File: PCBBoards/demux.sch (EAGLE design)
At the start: 106 parts, among them IC1 4013N, IC2 4013N, IC3 4013N, IC4 4013N, IC5 4013N, IC6 4013N, IC7 4069N, IC8 4069N, Q1 2N3904, Q10 2N3904, Q11 2N3904, Q12 2N3904, Q2 2N3904, Q3 2N3904, Q4 2N3904, Q5 2N3904, Q6 2N3904, Q7 2N3904, Q8 2N3904, Q9 2N3904, T1 2N3904, T2 2N3904, T3 2N3904, T4 2N3904, T5 2N3904, T6 2N3904

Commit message: fr/sr another one
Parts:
- removed C2, C3, C4, C5, C6, C7, C8, C9: 100n, rcl:C-EU050-035X075
- C1: value 100n -> 1u
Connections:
- new net N$80: IC6B.CLK, IC8D.O
- new net N$81: IC8D.I
- net +5V: no longer C2.1, C3.1, C4.1, C5.1, C6.1, C7.2, C8.1, C9.1
- net GND: no longer C2.2, C3.2, C4.2, C5.2, C6.2, C7.1, C8.2, C9.2
- net N$11: now also IC5B.CLK; no longer IC6B.CLK
- net N$2: now also IC7F.O; no longer IC7D.O
- net N$27: now also IC7F.I; no longer IC7D.I
- net N$29: now also IC7D.I; no longer IC7F.I
- net N$33: no longer IC8D.I
- net N$35: no longer IC8F.I
- net N$5: now also IC7D.O; no longer IC7F.O
- net N$9: now also IC8F.I; no longer IC5B.CLK, IC8D.O
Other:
- moved on the sheet: IC7D, IC7F, IC8D, IC8F

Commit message: first version of complited FR/SR PCB board
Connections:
- removed net N$24: IC7A.I, V11.0
- removed net N$3 (its old number): IC2A.CLK, IC7C.O
- removed net N$80: IC6B.CLK, IC8D.O
- removed net N$81: IC8D.I
- new net N$4: IC1A.CLK, IC7E.O
- new net N$82: IC8E.I, V11.8
- net N$1: now also IC2A.CLK, IC7F.O; no longer IC3A.CLK, IC7E.O
- net N$10: now also IC8B.I, V11.9; no longer IC6A.CLK, IC8E.O
- net N$11: now also IC6A.CLK, IC8D.O; no longer IC5B.CLK, IC8F.O
- net N$13: now also IC3B.CLK, IC7C.O; no longer IC1A.CLK, IC7A.O
- net N$2: now also IC7A.O; no longer IC7F.O
- net N$26: now also IC7F.I; no longer IC7C.I
- net N$27: now also IC7A.I; no longer IC7F.I
- net N$28: now also IC7D.I; no longer IC7E.I
- net N$29: now also IC7C.I; no longer IC7D.I
- net N$30: now also IC8F.I; no longer IC8A.I
- net N$31: now also IC8A.I; no longer IC8B.I
- net N$32: now also IC5B.CLK, IC8B.O; no longer IC8C.I, V11.8
- net N$33: now also IC5A.CLK, IC8E.O; no longer V11.9
- net N$34: now also IC8D.I; no longer IC8E.I
- net N$35: now also IC8C.I
- net N$5: now also IC7E.I, V11.0; no longer IC3B.CLK, IC7D.O
- net N$6: now also IC8F.O; no longer IC8A.O
- net N$7: now also IC8A.O; no longer IC8B.O
- net N$8: now also IC3A.CLK, IC7D.O; no longer IC5A.CLK, IC8C.O
- net N$9: now also IC6B.CLK, IC8C.O; no longer IC8F.I
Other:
- moved on the sheet: IC7A, IC7B, IC7C, IC7D, IC7E, IC7F, IC8A, IC8B, IC8C, IC8D, IC8E, IC8F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

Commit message: FR/RS Board one of final update
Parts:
- added C2, C3, C4, C5, C6, C7, C8, C9: 100n, rcl:C-EU025-025X050
- C1: value 1u -> 100n; device rcl:C-EU050-035X075 -> rcl:C-EU025-025X050
- R19, R24, R25, R28, R33, R34: value 15k -> 4.7k
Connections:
- net +5V: now also C2.1, C3.1, C4.1, C5.1, C6.1, C7.1, C8.1, C9.1
- net GND: now also C2.2, C3.2, C4.2, C5.2, C6.2, C7.2, C8.2, C9.2

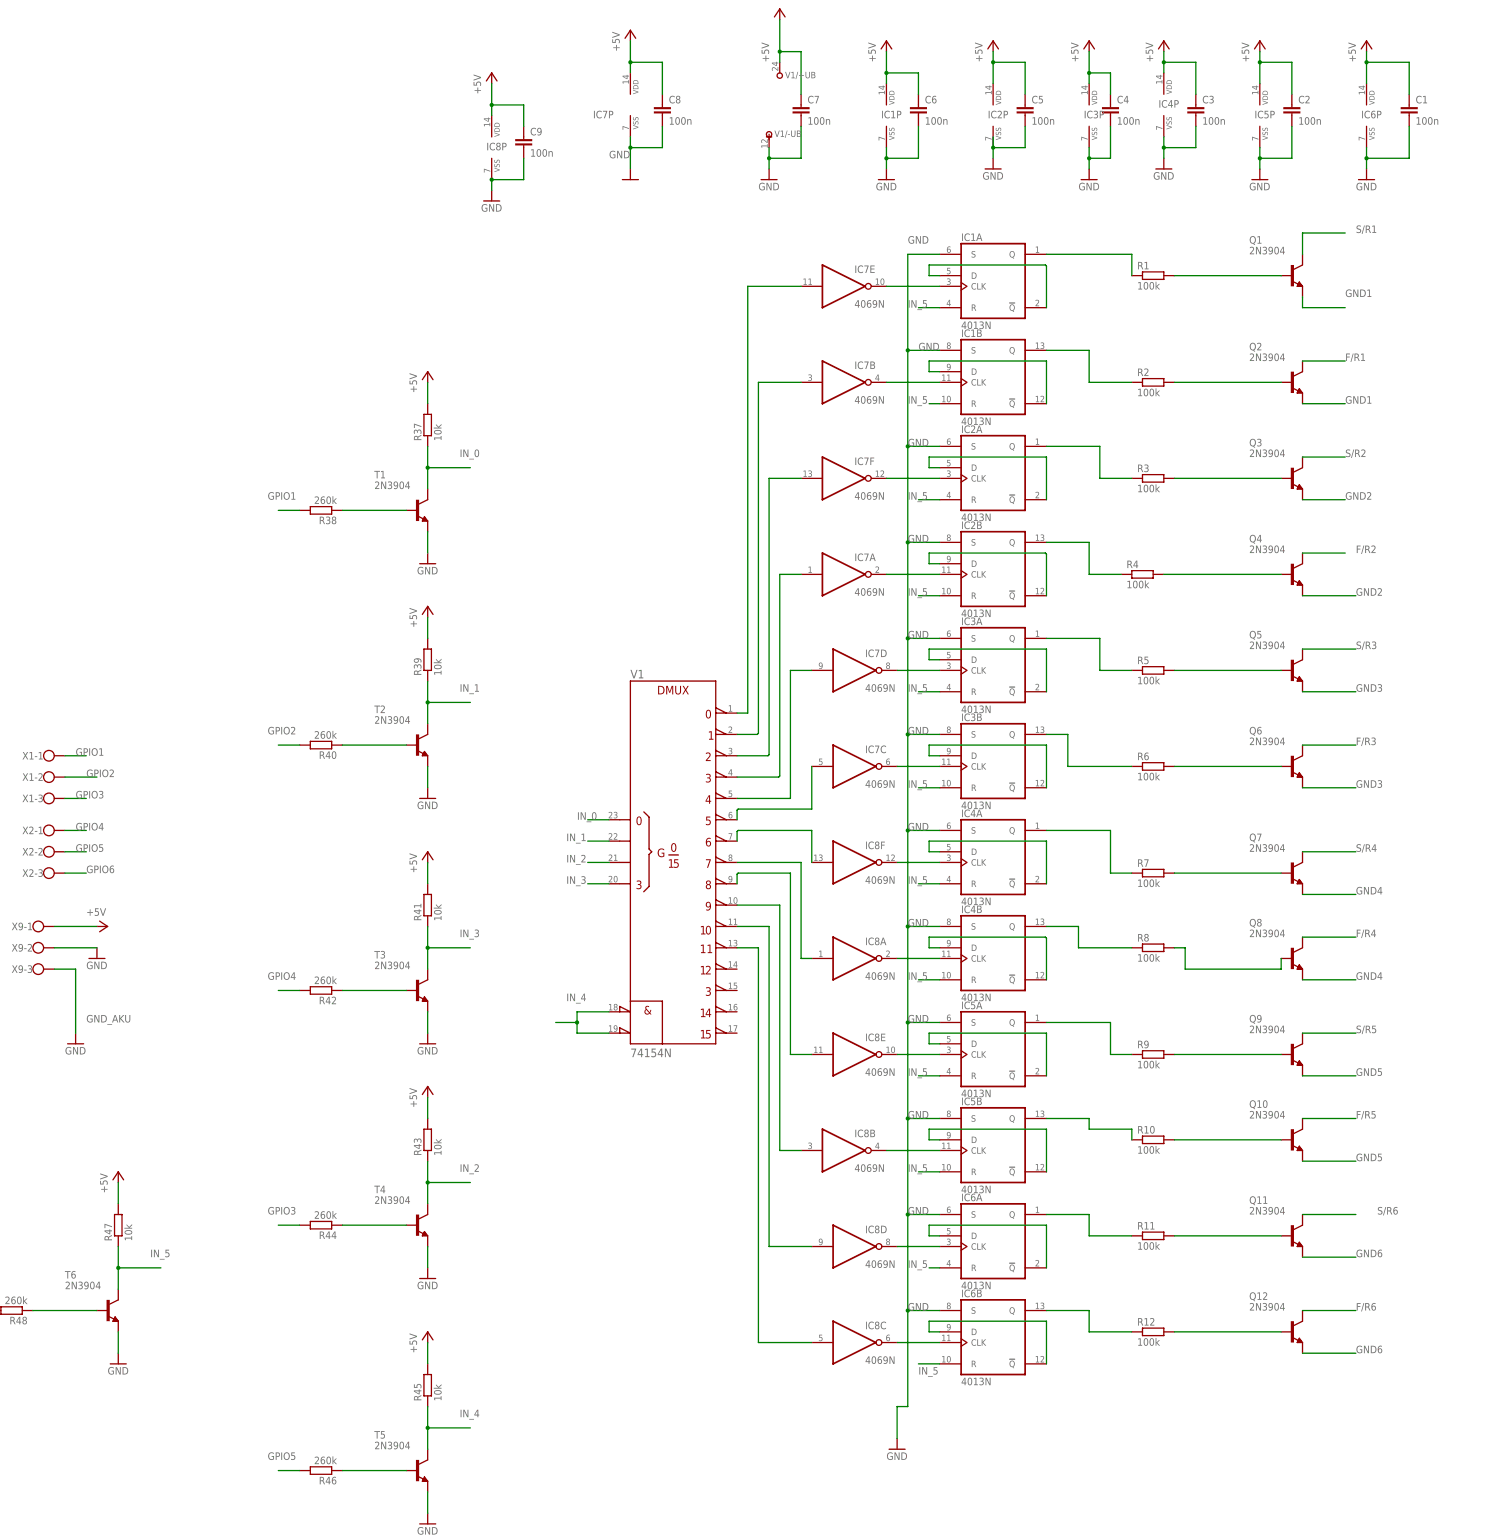
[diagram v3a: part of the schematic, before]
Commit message: FR/SR updated to 74HC**
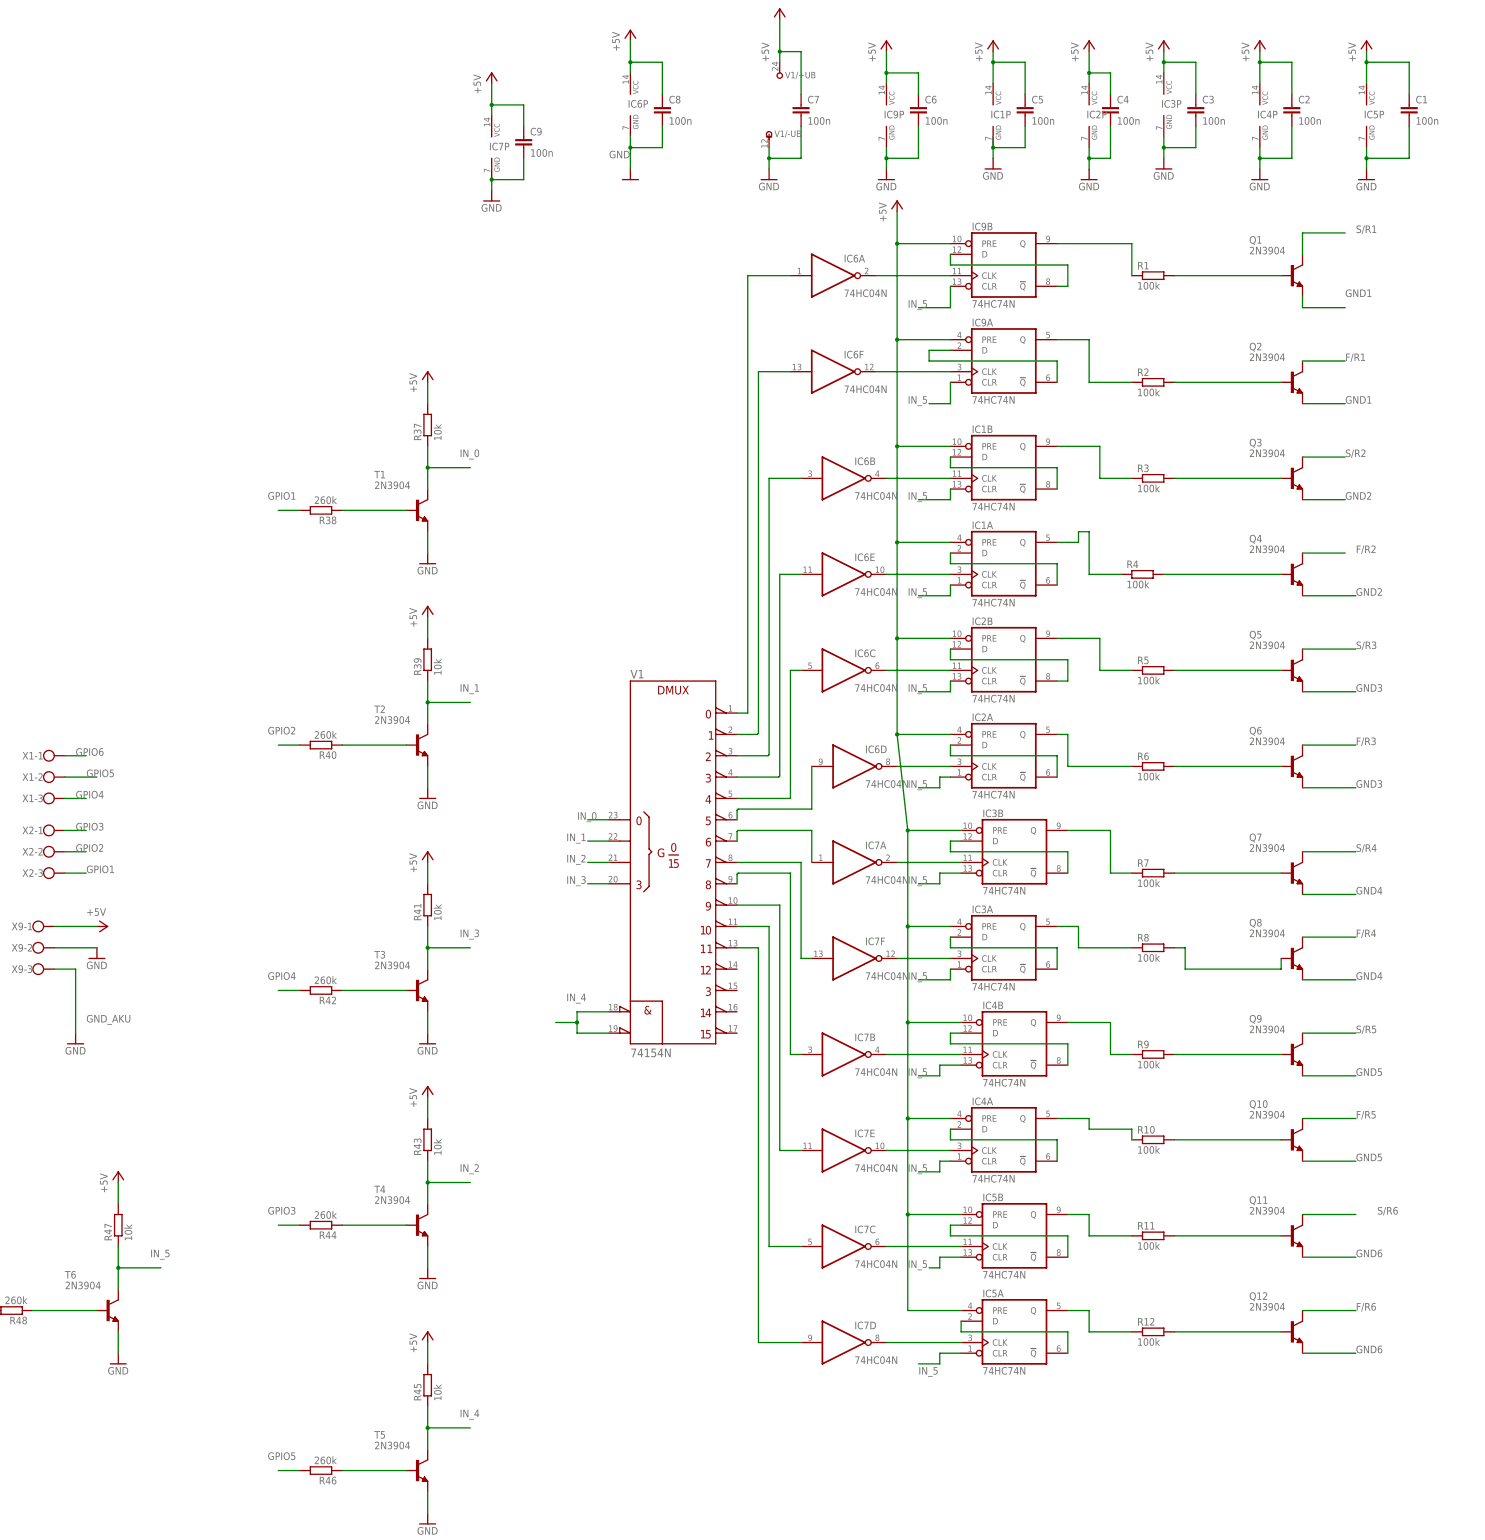
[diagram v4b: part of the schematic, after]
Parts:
- removed IC8: 4069N, 40xx:4069N
- added IC9: 74HC74N, 74xx-eu:74HC74N
- IC1, IC2, IC3, IC4, IC5: value 4013N -> 74HC74N; device 40xx:4013N -> 74xx-eu:74HC74N
- IC6: value 4013N -> 74HC04N; device 40xx:4013N -> 74xx-eu:74HC04N
- IC7: value 4069N -> 74HC04N; device 40xx:4069N -> 74xx-eu:74HC04N
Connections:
- removed net N$2 (its old number): IC2B.CLK, IC7A.O
- removed net N$32 (its old number): IC5B.CLK, IC8B.O
- removed net N$33 (its old number): IC5A.CLK, IC8E.O
- removed net N$36: IC6B.!Q, IC6B.D
- removed net N$6 (its old number): IC4A.CLK, IC8F.O
- removed net N$7 (its old number): IC4B.CLK, IC8A.O
- removed net N$8 (its old number): IC3A.CLK, IC7D.O
- removed net N$9 (its old number): IC6B.CLK, IC8C.O
- new net N$12: IC6F.O, IC9A.CLK
- new net N$14: IC9A.!Q, IC9A.D
- new net N$15: IC1B.CLK, IC6B.O
- new net N$16: IC5B.CLK, IC7C.O
- new net N$17: IC3B.CLK, IC7A.O
- new net N$19: IC3A.CLK, IC7F.O
- new net N$22: IC2A.CLK, IC6D.O
- new net N$24: IC1A.CLK, IC6E.O
- net +5V: now also IC1A.PRE, IC1B.PRE, IC1P.VCC, IC2A.PRE, IC2B.PRE, IC2P.VCC, IC3A.PRE, IC3B.PRE, IC3P.VCC, IC4A.PRE, IC4B.PRE, IC4P.VCC, IC5A.PRE, IC5B.PRE, IC5P.VCC, IC6P.VCC, IC7P.VCC, IC9A.PRE, IC9B.PRE, IC9P.VCC; no longer IC1P.VDD, IC2P.VDD, IC3P.VDD, IC4P.VDD, IC5P.VDD, IC6P.VDD, IC7P.VDD, IC8P.VDD
- net GND: now also IC1P.GND, IC2P.GND, IC3P.GND, IC4P.GND, IC5P.GND, IC6P.GND, IC7P.GND, IC9P.GND; no longer IC1A.S, IC1B.S, IC1P.VSS, IC2A.S, IC2B.S, IC2P.VSS, IC3A.S, IC3B.S, IC3P.VSS, IC4A.S, IC4B.S, IC4P.VSS, IC5A.S, IC5B.S, IC5P.VSS, IC6A.S, IC6B.S, IC6P.VSS, IC7P.VSS, IC8P.VSS
- net GPIO1: now also X2-3.KL; no longer X1-1.KL
- net GPIO2: now also X2-2.KL; no longer X1-2.KL
- net GPIO3: now also X2-1.KL; no longer X1-3.KL
- net GPIO4: now also X1-3.KL; no longer X2-1.KL
- net GPIO5: now also X1-2.KL; no longer X2-2.KL
- net GPIO6: now also X1-1.KL; no longer X2-3.KL
- net IN_5: now also IC1A.CLR, IC1B.CLR, IC2A.CLR, IC2B.CLR, IC3A.CLR, IC3B.CLR, IC4A.CLR, IC4B.CLR, IC5A.CLR, IC5B.CLR, IC9A.CLR, IC9B.CLR; no longer IC1A.R, IC1B.R, IC2A.R, IC2B.R, IC3A.R, IC3B.R, IC4A.R, IC4B.R, IC5A.R, IC5B.R, IC6A.R, IC6B.R
- net N$1: now also IC4B.CLK, IC7B.O; no longer IC2A.CLK, IC7F.O
- net N$10: now also IC7E.I; no longer IC8B.I
- net N$11: now also IC4A.CLK, IC7E.O; no longer IC6A.CLK, IC8D.O
- net N$13: now also IC5A.CLK, IC7D.O; no longer IC3B.CLK, IC7C.O
- net N$23: now also IC2B.CLK, IC6C.O; no longer IC6A.!Q, IC6A.D
- net N$25: now also IC6F.I; no longer IC7B.I
- net N$26: now also IC6B.I; no longer IC7F.I
- net N$27: now also IC6E.I; no longer IC7A.I
- net N$28: now also IC6C.I; no longer IC7D.I
- net N$29: now also IC6D.I; no longer IC7C.I
- net N$3: now also IC9B.!Q, IC9B.D; no longer IC1B.CLK, IC7B.O
- net N$30: now also IC7A.I; no longer IC8F.I
- net N$31: now also IC7F.I; no longer IC8A.I
- net N$34: now also IC7C.I; no longer IC8D.I
- net N$35: now also IC7D.I; no longer IC8C.I
- net N$37: now also IC9B.Q; no longer IC1A.Q
- net N$4: now also IC6A.O, IC9B.CLK; no longer IC1A.CLK, IC7E.O
- net N$40: now also IC9A.Q; no longer IC1B.Q
- net N$41: now also IC1B.Q; no longer IC2A.Q
- net N$44: now also IC1A.Q; no longer IC2B.Q
- net N$45: now also IC2B.Q; no longer IC3A.Q
- net N$48: now also IC2A.Q; no longer IC3B.Q
- net N$49: now also IC3B.Q; no longer IC4A.Q
- net N$5: now also IC6A.I; no longer IC7E.I
- net N$52: now also IC3A.Q; no longer IC4B.Q
- net N$53: now also IC4B.Q; no longer IC5A.Q
- net N$56: now also IC4A.Q; no longer IC5B.Q
- net N$57: now also IC5B.Q; no longer IC6A.Q
- net N$60: now also IC5A.Q; no longer IC6B.Q
- net N$82: now also IC7B.I; no longer IC8E.I
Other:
- moved on the sheet: IC1P, IC2P, IC3P, IC4P, IC5P, IC6P, IC7A, IC7B, IC7C, IC7D, IC7E, IC7F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
